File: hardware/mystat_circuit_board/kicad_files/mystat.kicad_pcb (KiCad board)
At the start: 4 copper layers, 60 x 81 mm, 93 parts, among them J1 PJ-063AH, J4 Screw_Terminal_01x04, P1 ICSP, U10 OPA192, U11 BUF634AIDDAR, U12 ADG1419, U13 OPA192, U14 OPA192, U15 OPA192, U16 OPA192, U17 OPA192, U2 LTM8045, U3 ADP7182AUJZ-R7, U4 ADP7118AUJZ-5.0-R7, U5 PIC16F1459, U6 ADR421, U7 MCP3551, U8 MCP3551, U9 DAC1220, X1 2.5 MHz

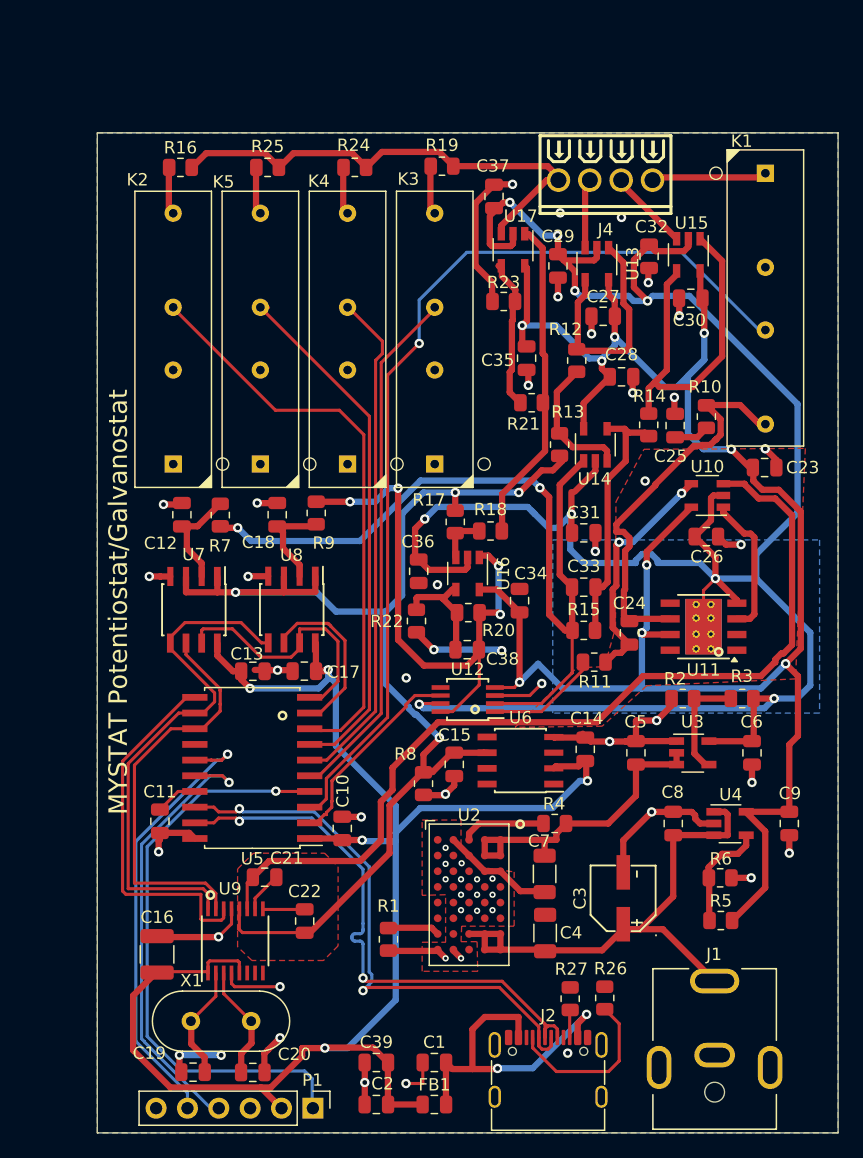
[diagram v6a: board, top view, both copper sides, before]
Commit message: change relays back to original tdstat, re-add GND connection, add changelog from now on
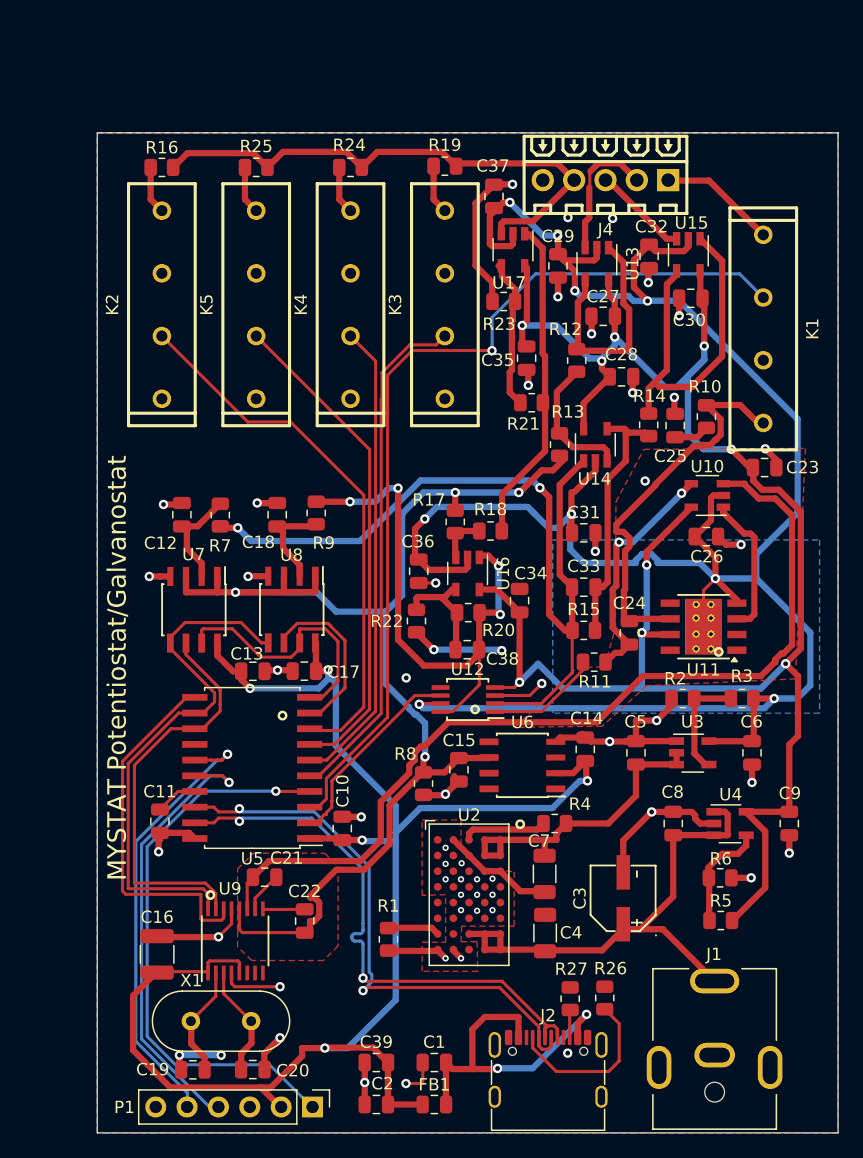
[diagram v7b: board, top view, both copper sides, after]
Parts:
- J4: footprint easyeda2kicad:CONN-TH_4P-P2.54_MX128-2.54-GN01-04P-CU-Y-A -> easyeda2kicad:CONN-TH_5P-P2.54_MX128-2.54-05P-GN01-CU-Y-A
- K1, K2, K3, K4, K5: footprint my_footprints:Reed_Relay_MiRelay_SIP-HV1A05D -> easyeda2kicad:SIP-4_L19.6-W5.4-P5.08_9007-SPST-NO
- moved K2 12.9 mm to (55.2, 63.9)
- moved K3 12.9 mm to (78.2, 63.9)
- moved K5 12.9 mm to (62.9, 63.9)
- moved K4 12.9 mm to (70.5, 63.9)
- moved K1 12.6 mm to (103.9, 65.9)
- moved R16 1.50 mm to (55.2, 52.8)
- moved R25 0.92 mm to (62.9, 52.8)
- moved C15 0.58 mm to (79.3, 101.6)
- moved U6 0.42 mm to (84.4, 101.2)
- moved R24 0.35 mm to (70.5, 52.8)
- moved R19 0.23 mm to (78.2, 52.7)
- moved C20 0.23 mm to (62.6, 125.9)
- moved C19 0.19 mm to (57.7, 125.9)
- moved P1 0.10 mm to (67.4, 128.9)
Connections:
- J4 pad 2: RE -> SE
- J4 pad 3: SE -> RE
- K1 pad 2: GND -> CELL_ON
- K1 pad 3: CELL_ON -> GND
- K2 pad 2: GND -> RANGE4
- K2 pad 3: RANGE4 -> GND
- K3 pad 2: GND -> RANGE3
- K3 pad 3: RANGE3 -> GND
- K4 pad 2: GND -> RANGE2
- K4 pad 3: RANGE2 -> GND
- K5 pad 2: GND -> RANGE1
- K5 pad 3: RANGE1 -> GND
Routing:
- net SE: track 5.73 -> 11.0 mm
- net CE: track 40.4 -> 44.5 mm
- net RANGE4: track 46.1 -> 43.2 mm
- net RANGE2: track 40.3 -> 37.5 mm
- net RANGE1: track 42.2 -> 39.3 mm
- net CELL_ON: track 76.2 -> 73.5 mm
- net RE: track 5.97 -> 7.73 mm
- net Vref: track 98.1 -> 99.7 mm
- net Net-(P1-Pin_1): track 47.6 -> 46.2 mm
- net WE: track 8.30 -> 9.53 mm
- net -13.4V: track 186.8 -> 185.7 mm
- net Net-(P1-Pin_4): track 36.3 -> 36.9 mm
- net RANGE3: track 41.7 -> 41.1 mm
- net Net-(K5-Pad4): track 3.85 -> 4.37 mm
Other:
- board text added: "CE"
- board text added: "GND"
- board text added: "RE"
- board text added: "SE"
- board text added: "WE"
